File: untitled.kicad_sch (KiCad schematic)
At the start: 21 parts, among them J1 Conn_02x13_Top_Bottom, J12 Conn_01x03_Pin, J2 Conn_01x13, J3 Conn_02x06_Odd_Even, P1 USB_C_Receptacle_USB2.0, U4 BC847BDW1T1G, U5 CP2102N-A02-GQFN28

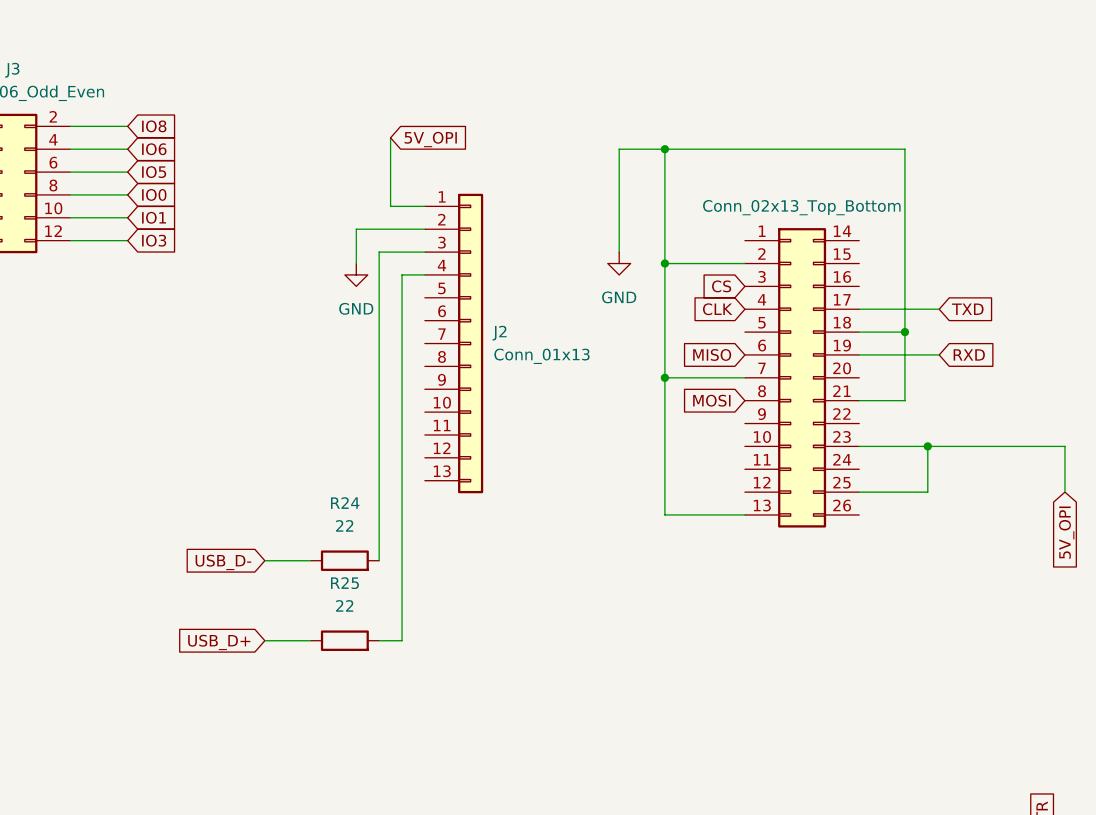
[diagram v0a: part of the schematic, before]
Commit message: Start v4 layout on Raspberry Pi HAT outline
Clear the v3.1 layout down to a 65x56 mm HAT board outline with the four
M3 mounting holes, ready for fresh placement. Update the schematic and
CLAUDE.md for the Raspberry Pi 40-pin header.

Co-Authored-By: Claude Opus 5.5 <noreply@anthropic.com>
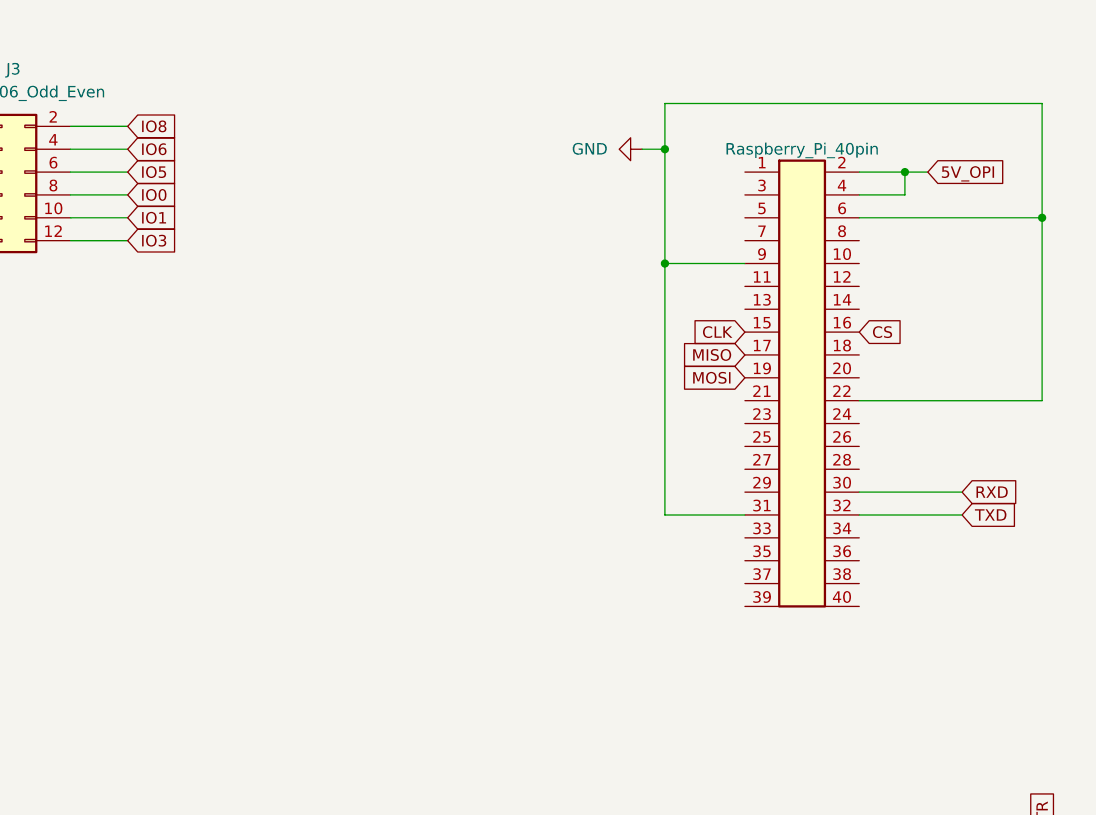
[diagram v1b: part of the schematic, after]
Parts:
- removed J2: Conn_01x13, Connector_PinSocket_2.54mm:PinSocket_1x13_P2.54mm_Vertical, symbol Connector_Generic:Conn_01x13
- removed R24, R25: 22, Resistor_SMD:R_0603_1608Metric, symbol Device:R
- J1: value Conn_02x13_Top_Bottom -> Raspberry_Pi_40pin; footprint Connector_PinSocket_2.54mm:PinSocket_2x13_P2.54mm_Vertical -> Connector_PinSocket_2.54mm:PinSocket_2x20_P2.54mm_Vertical; symbol Connector_Generic:Conn_02x13_Top_Bottom -> Connector_Generic:Conn_02x20_Odd_Even
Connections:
- net 5V_OPI: now also J1.2 (Pin_2), J1.4 (Pin_4); no longer J1.23 (Pin_23), J1.25 (Pin_25)
- net CLK: now also J1.15 (Pin_15); no longer J1.4 (Pin_4)
- net CS: now also J1.16 (Pin_16); no longer J1.3 (Pin_3)
- net GND: now also J1.22 (Pin_22), J1.31 (Pin_31), J1.6 (Pin_6), J1.9 (Pin_9); no longer J1.13 (Pin_13), J1.18 (Pin_18), J1.2 (Pin_2), J1.21 (Pin_21), J1.7 (Pin_7)
- net MISO: now also J1.17 (Pin_17); no longer J1.6 (Pin_6)
- net MOSI: now also J1.19 (Pin_19); no longer J1.8 (Pin_8)
- net RXD: now also J1.30 (Pin_30); no longer J1.19 (Pin_19)
- net TXD: now also J1.32 (Pin_32); no longer J1.17 (Pin_17)

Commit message: Rework v4 schematic for Raspberry Pi 4/5 HAT
- Remap J1 to the Raspberry Pi 40-pin pinout (was still Orange Pi pin
  numbers: Pi 3V3 on MISO, GND on ESP32 RX)
- Fix auto-reset: U4 collectors drove EN and IO9 the wrong way round
- Let the Pi flash the ESP32: UART via 74LVC1G08 AND gate (U10) shared
  with the CP2102N, EN/BOOT on GPIO5/6 through 1k; add IO9 pull-up
- Power the Pi straight from +5V, drop the SS34 diode (D6)
- Add fan control: AO3400A low-side switch on GPIO18, tach on GPIO24
- Move mux LEDs D1-D3 off strapping pin GPIO8 to the 5V select lines
- Add 3V3 power LED and test points TP8-TP33
- Document v4 in CLAUDE.md

Co-Authored-By: Claude Opus 5.5 <noreply@anthropic.com>
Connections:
- net 5V_OPI is gone; now on net +5V: J1.2 (Pin_2), J1.4 (Pin_4)
- net CHIP_UP: now also U4.3 (COLLECTOR1); no longer U4.6 (COLLECTOR2)
- net CLK: now also J1.23 (Pin_23); no longer J1.15 (Pin_15)
- net CS: now also J1.24 (Pin_24); no longer J1.16 (Pin_16)
- net GND: now also J1.14 (Pin_14), J1.20 (Pin_20), J1.25 (Pin_25), J1.30 (Pin_30), J1.34 (Pin_34), J1.39 (Pin_39); no longer J1.22 (Pin_22), J1.31 (Pin_31)
- net IO9: now also U4.6 (COLLECTOR2); no longer U4.3 (COLLECTOR1)
- net MISO: now also J1.21 (Pin_21); no longer J1.17 (Pin_17)
- net TXD: now also J1.10 (Pin_10); no longer J1.32 (Pin_32)
- net FAN_PWM: now reaches J1.12 (Pin_12)
- net FAN_TACH: now reaches J1.18 (Pin_18)
- net PI_EN: now reaches J1.29 (Pin_29)
- net PI_TX: now reaches J1.8 (Pin_8)
- net RXD renamed USB_TX
- net USB_TX: no longer J1.30 (Pin_30)
- new net PI_BOOT: J1.31 (Pin_31)
- no-connect marks 18 -> 38

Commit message: Add first v4 HAT layout (4 layers, autorouted draft)
- 65x56 mm Raspberry Pi HAT outline, J1 on the bottom at the Pi position
- 4 layers: signal + GND pour on outer layers, In1 GND plane, In2 +5V plane,
  GND stitching vias
- Locked wide power tracks from the screw terminals to the JST outputs and
  to the Pi 5V pins; net classes for power and 3V3
- Address LEDs D1-D3 in one row, power LEDs next to the power input
- Autorouted with Freerouting; 8 connections, 3 edge clearances and the
  silkscreen still need hand work
- Add PWR_FLAG to +5V and GND, remove a stray no-connect (ERC clean)

Co-Authored-By: Claude Opus 5.5 <noreply@anthropic.com>
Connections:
- no-connect marks 38 -> 37
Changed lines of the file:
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@@
   (no_connect (at 82.55 138.43))
   (no_connect (at 128.27 138.43))
-  (no_connect (at -22.86 15.24))
   (no_connect (at 41.91 82.55))
   (no_connect (at 128.27 140.97))
